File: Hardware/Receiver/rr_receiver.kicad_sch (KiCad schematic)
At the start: 17 parts, among them J1 TX, J2 SERVO1, J3 POWER, J4 SERVO2, J5 ICSP, U1 AMS1117-3.3, U2 ATmega328P-A, U3 NRF24L01_Breakout, Y1 16MHz

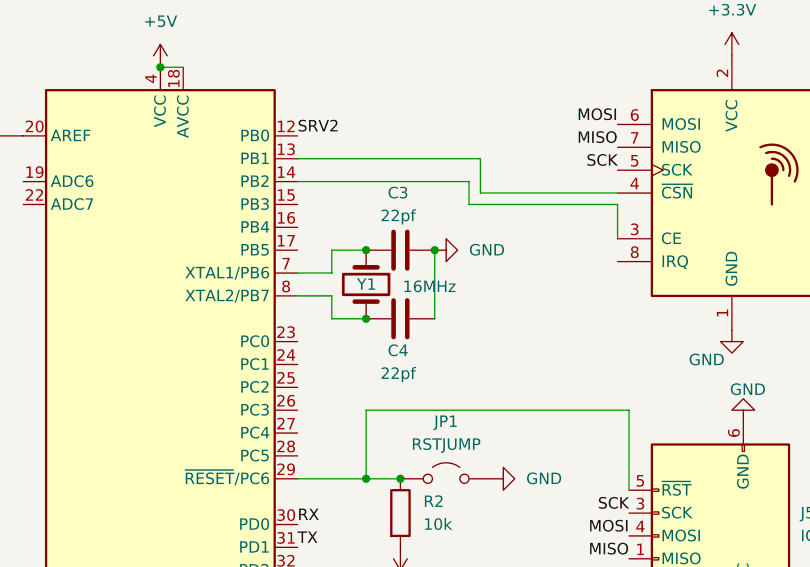
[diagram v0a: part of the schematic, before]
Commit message: update receiver because the old one doesn't work
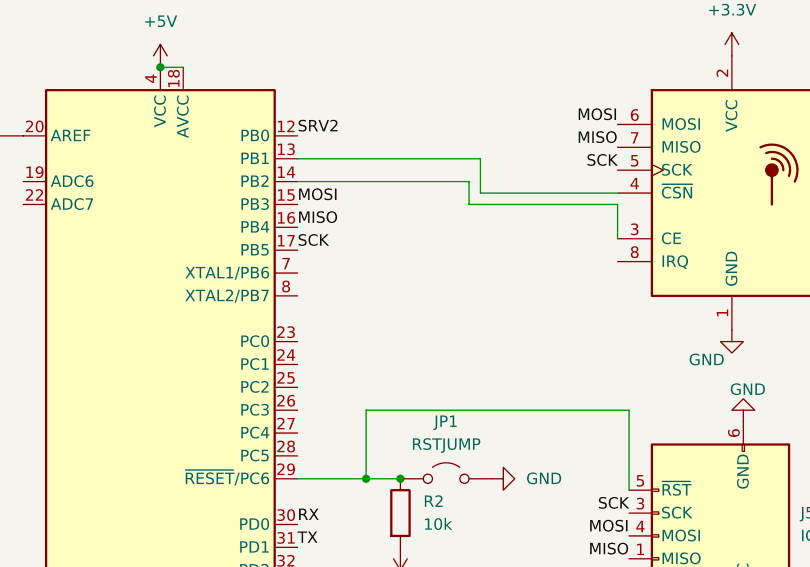
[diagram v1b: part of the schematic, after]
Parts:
- removed C3, C4: 22pf, Capacitor_SMD:C_0805_2012Metric, symbol Device:C
- removed Y1: 16MHz, Crystal:Crystal_SMD_HC49-SD, symbol Device:Crystal
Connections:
- net MISO: now also U2.16 (PB4)
- net MOSI: now also U2.15 (PB3)
- net SCK: now also U2.17 (PB5)
